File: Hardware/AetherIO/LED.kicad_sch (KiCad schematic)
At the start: 4 parts

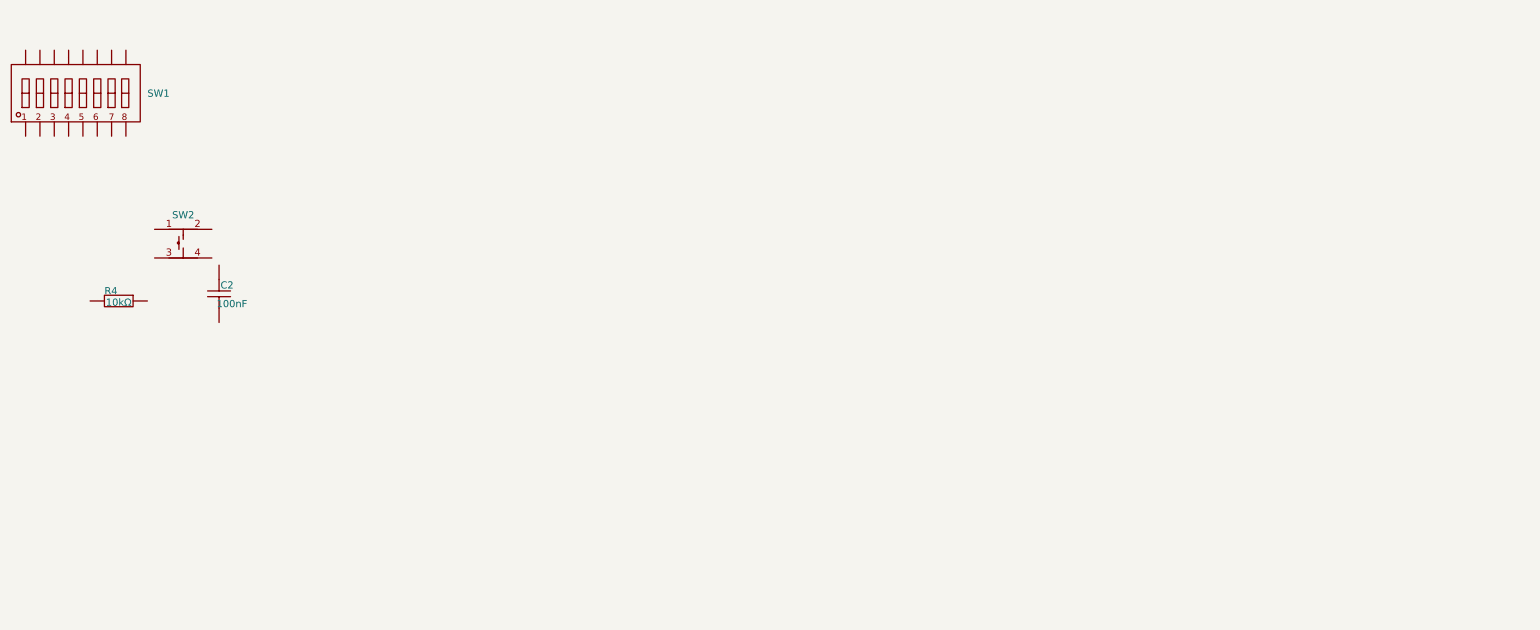
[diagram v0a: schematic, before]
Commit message: add new key and filter design
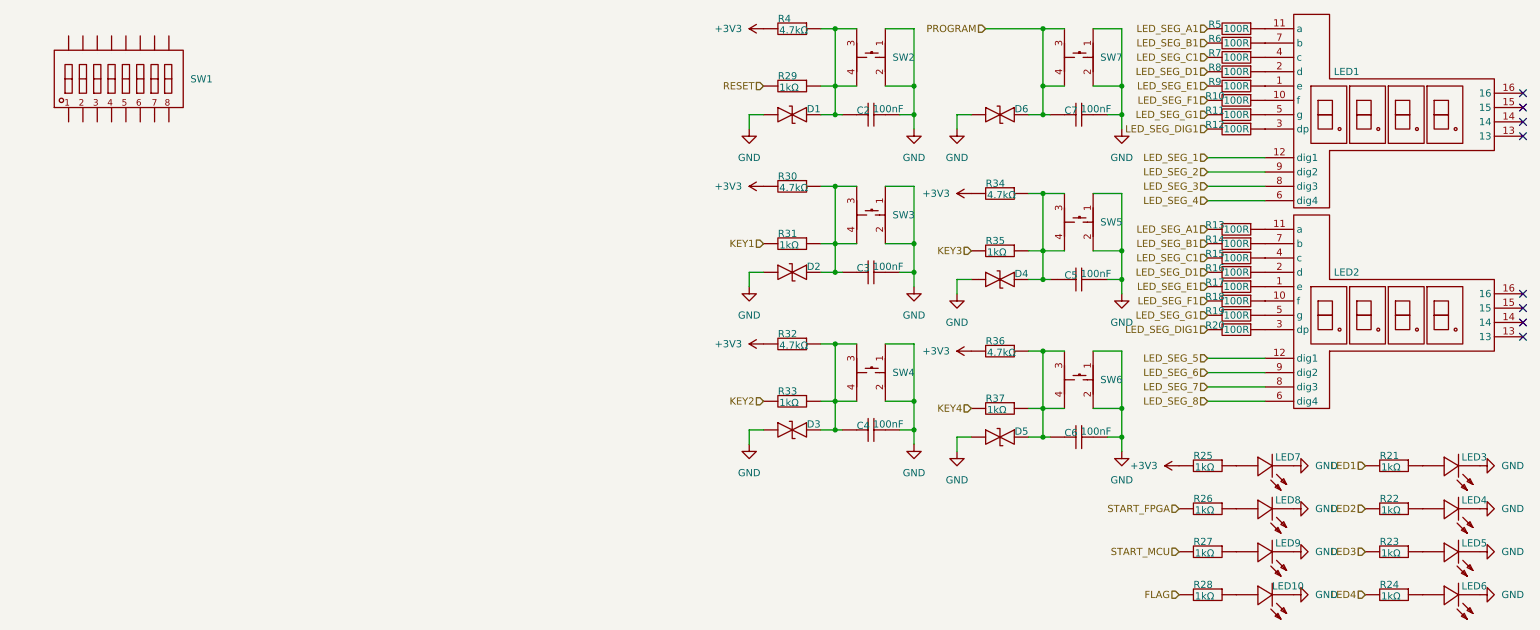
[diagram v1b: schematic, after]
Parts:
- added C3, C4, C5, C6, C7: 100nF, persional_library:C0603, symbol persional_library:C0603
- added D1, D2, D3, D4, D5, D6: ~, persional_library:SOD-323_L1.8-W1.3-LS2.5-BI, symbol persional_library:ESD_PESD3V3L1BA-N
- added LED1, LED2: ~, persional_library:GS2040, symbol persional_library:SEG_20-4S
- added LED10, LED3, LED4, LED5, LED6, LED7, LED8, LED9: ~, persional_library:LED0603-RD, symbol persional_library:LED0603
- added R10, R11, R12, R13, R14, R15, R16, R17, R18, R19, R20, R5, R6, R7, R8, R9: 100R, persional_library:R0603, symbol persional_library:R0603
- added R21, R22, R23, R24, R25, R26, R27, R28, R29, R31, R33, R35, R37: 1kΩ, persional_library:R0603, symbol persional_library:R0603
- added R30, R32, R34, R36: 4.7kΩ, persional_library:R0603, symbol persional_library:R0603
- added SW3, SW4, SW5, SW6, SW7: ~, persional_library:SW-SMD_4P-L4.2-W3.2-P2.15-LS4.6-1, symbol persional_library:Switch_PushButton_TS3425BA
- R4: value 10kΩ -> 4.7kΩ
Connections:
- net at R4.1: now also C2.1, SW2.3, SW2.4, D1.2, R29.1
- net +3V3: now reaches R4.2
- net +3V3: now also R25.2, R30.2, R32.2, R34.2, R36.2
- net GND: now reaches C2.2
- net GND: now also SW2.1, SW2.2, C3.2, C4.2, C5.2, C6.2, C7.2, D1.1, D2.1, D3.1, D4.1, D5.1, D6.1, LED10.1 (-), LED3.1 (-), LED4.1 (-), LED5.1 (-), LED6.1 (-), LED7.1 (-), LED8.1 (-), LED9.1 (-), SW3.1, SW3.2, SW4.1, SW4.2, SW5.1, SW5.2, SW6.1, SW6.2, SW7.1, SW7.2
- new net: C4.1, D3.2, R32.1, R33.1, SW4.3, SW4.4
- new net: LED2.5 (g), R19.1
- new net: LED1.3 (dp), R12.1
- new net: LED4.2 (+), R22.1
- new net: LED7.2 (+), R25.1
- new net: C6.1, D5.2, R36.1, R37.1, SW6.3, SW6.4
- new net: C5.1, D4.2, R34.1, R35.1, SW5.3, SW5.4
- new net: LED8.2 (+), R26.1
- new net: LED2.7 (b), R14.1
- new net: LED1.11 (a), R5.1
- new net: LED9.2 (+), R27.1
- new net: LED1.1 (e), R9.1
- new net: LED1.10 (f), R10.1
- new net: LED1.2 (d), R8.1
- new net: LED1.4 (c), R7.1
- new net: LED1.5 (g), R11.1
- new net: LED1.7 (b), R6.1
- new net: LED2.1 (e), R17.1
- new net: LED2.10 (f), R18.1
- new net: LED2.11 (a), R13.1
- new net: LED2.2 (d), R16.1
- new net: LED2.3 (dp), R20.1
- new net: LED2.4 (c), R15.1
- new net: LED5.2 (+), R23.1
- new net: C3.1, D2.2, R30.1, R31.1, SW3.3, SW3.4
- new net: LED3.2 (+), R21.1
- new net: LED6.2 (+), R24.1
- new net: LED10.2 (+), R28.1
- new net FLAG: R28.2
- new net KEY1: R31.2
- new net KEY2: R33.2
- new net KEY3: R35.2
- new net KEY4: R37.2
- new net LED1: R21.2
- new net LED2: R22.2
- new net LED3: R23.2
- new net LED4: R24.2
- new net LED_SEG_1: LED1.12 (dig1)
- new net LED_SEG_2: LED1.9 (dig2)
- new net LED_SEG_3: LED1.8 (dig3)
- new net LED_SEG_4: LED1.6 (dig4)
- new net LED_SEG_5: LED2.12 (dig1)
- new net LED_SEG_6: LED2.9 (dig2)
- new net LED_SEG_7: LED2.8 (dig3)
- new net LED_SEG_8: LED2.6 (dig4)
- new net LED_SEG_A1: R13.2, R5.2
- new net LED_SEG_B1: R14.2, R6.2
- new net LED_SEG_C1: R15.2, R7.2
- new net LED_SEG_D1: R16.2, R8.2
- new net LED_SEG_DIG1: R12.2, R20.2
- new net LED_SEG_E1: R17.2, R9.2
- new net LED_SEG_F1: R10.2, R18.2
- new net LED_SEG_G1: R11.2, R19.2
- new net PROGRAM: C7.1, D6.2, SW7.3, SW7.4
- new net RESET: R29.2
- new net START_FPGA: R26.2
- new net START_MCU: R27.2
- no-connect marks 0 -> 8
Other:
- moved on the sheet: C2, R4, SW1, SW2
